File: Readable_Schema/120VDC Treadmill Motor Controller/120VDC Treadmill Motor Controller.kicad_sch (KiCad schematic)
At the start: 0 parts

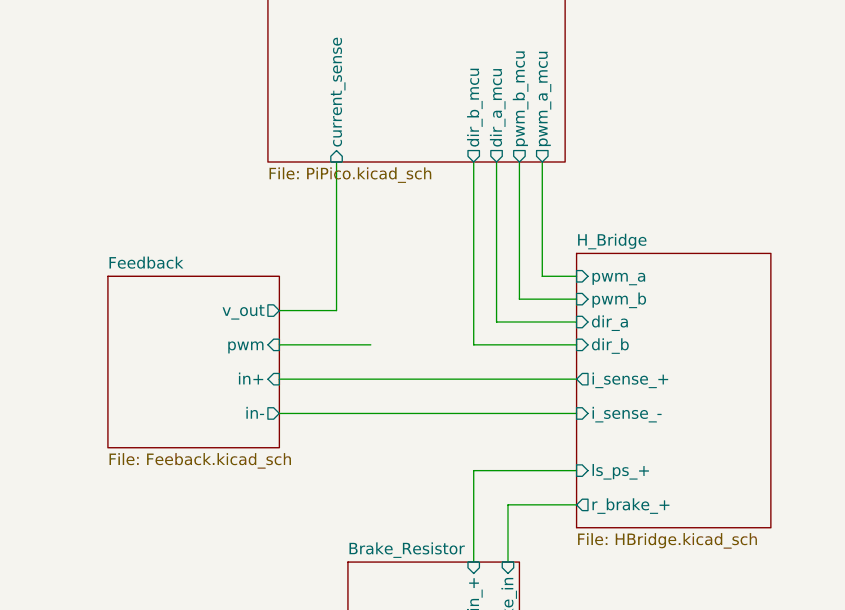
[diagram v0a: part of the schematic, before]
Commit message: -Tried to fix a decent portion of the feedback circuit. Basically the new gate drivers have a enable pin so it makes more sense to tie the OC pin directly to the function of EN. Also kept the SR latch as a method of delaying the restart and avoiding hysterysis -Still working through the brake resistor subcircuit, basically switching all comparator logic to HV and thinking of using optoisolation to feed comparator output to the gate driver to keep things isolated. Truthfully feels like I should just nuke that FOD3182 and use a bootstrap or something else since I could care less about isolation in that subcircuit since no communication with the microcontroller is needed.
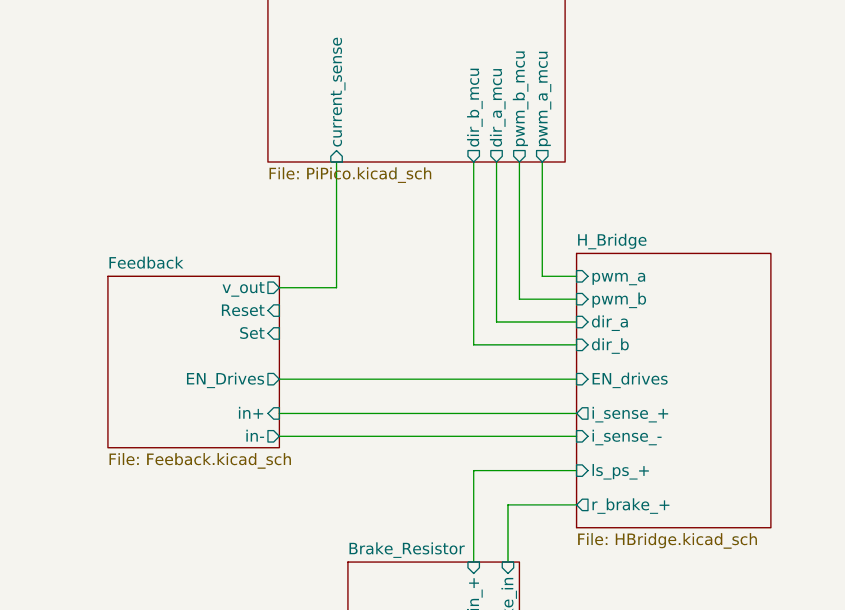
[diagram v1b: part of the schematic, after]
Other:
- sheet Feedback ports: added EN_Drives, Reset, Set; removed pwm
- sheet H_Bridge ports: added EN_drives; removed none
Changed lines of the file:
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@@
+	(wire
+		(pts
+			(xy 123.19 114.3) (xy 156.21 114.3)
+		)
+		(stroke
+			(width 0)
+			(type default)
+		)
+	)
+	(wire
+		(pts
+			(xy 123.19 97.79) (xy 129.54 97.79)
+		)
+		(stroke
+			(width 0)
+			(type default)
+		)
+	)
+	(wire
+		(pts
+			(xy 144.78 128.27) (xy 144.78 118.11)
+		)
+		(stroke
+			(width 0)
+			(type default)
+		)
+	)
+	(wire
+		(pts
+			(xy 144.78 104.14) (xy 156.21 104.14)
+		)
+		(stroke
+			(width 0)
+			(type default)
+		)
+	)
+	(wire
+		(pts
+			(xy 148.59 121.92) (xy 156.21 121.92)
+		)
+		(stroke
+			(width 0)
+			(type default)
+		)
+	)
+	(wire
+		(pts
+			(xy 152.4 83.82) (xy 152.4 96.52)
+		)
+		(stroke
+			(width 0)
+			(type default)
+		)
+	)
+	(wire
+		(pts
+			(xy 152.4 96.52) (xy 156.21 96.52)
+		)
+		(stroke
+			(width 0)
+			(type default)
+		)
+	)
+	(wire
+		(pts
+			(xy 147.32 101.6) (xy 156.21 101.6)
+		)
+		(stroke
+			(width 0)
+			(type default)
+		)
+	)
+	(wire
+		(pts
+			(xy 149.86 83.82) (xy 149.86 99.06)
+		)
+		(stroke
+			(width 0)
+			(type default)
+		)
+	)
+	(wire
+		(pts
+			(xy 144.78 83.82) (xy 144.78 104.14)
+		)
+		(stroke
+			(width 0)
+			(type default)
+		)
+	)
+	(wire
+		(pts
+			(xy 149.86 99.06) (xy 156.21 99.06)
+		)
+		(stroke
+			(width 0)
+			(type default)
+		)
+	)
+	(wire
+		(pts
+			(xy 147.32 83.82) (xy 147.32 101.6)
+		)
+		(stroke
+			(width 0)
+			(type default)
+		)
+	)
+	(wire
+		(pts
+			(xy 144.78 118.11) (xy 156.21 118.11)
+		)
+		(stroke
+			(width 0)
+			(type default)
+		)
+	)
+	(wire
+		(pts
+			(xy 129.54 83.82) (xy 129.54 97.79)
+		)
+		(stroke
+			(width 0)
+			(type default)
+		)
+	)
 	(wire
 		(pts
@@
 	(wire
 		(pts
-			(xy 123.19 100.33) (xy 129.54 100.33)
-		)
-		(stroke
-			(width 0)
-			(type default)
-		)
-	)
-	(wire
-		(pts
-			(xy 144.78 128.27) (xy 144.78 118.11)
-		)
-		(stroke
-			(width 0)
-			(type default)
-		)
-	)
-	(wire
-		(pts
-			(xy 144.78 104.14) (xy 156.21 104.14)
-		)
-		(stroke
-			(width 0)
-			(type default)
-		)
-	)
-	(wire
-		(pts
-			(xy 123.19 104.14) (xy 133.35 104.14)
-		)
-		(stroke
-			(width 0)
-			(type default)
-		)
-	)
-	(wire
-		(pts
-			(xy 148.59 121.92) (xy 156.21 121.92)
-		)
-		(stroke
-			(width 0)
-			(type default)
-		)
-	)
-	(wire
-		(pts
-			(xy 152.4 83.82) (xy 152.4 96.52)
-		)
-		(stroke
-			(width 0)
-			(type default)
-		)
-	)
-	(wire
-		(pts
-			(xy 152.4 96.52) (xy 156.21 96.52)
-		)
-		(stroke
-			(width 0)
-			(type default)
-		)
-	)
-	(wire
-		(pts
-			(xy 147.32 101.6) (xy 156.21 101.6)
-		)
-		(stroke
-			(width 0)
-			(type default)
-		)
-	)
-	(wire
-		(pts
-			(xy 149.86 83.82) (xy 149.86 99.06)
-		)
-		(stroke
-			(width 0)
-			(type default)
-		)
-	)
-	(wire
-		(pts
-			(xy 144.78 83.82) (xy 144.78 104.14)
-		)
-		(stroke
-			(width 0)
-			(type default)
-		)
-	)
-	(wire
-		(pts
-			(xy 149.86 99.06) (xy 156.21 99.06)
-		)
-		(stroke
-			(width 0)
-			(type default)
-		)
-	)
-	(wire
-		(pts
-			(xy 147.32 83.82) (xy 147.32 101.6)
+			(xy 148.59 128.27) (xy 148.59 121.92)
 		)
 		(stroke
@@
 		(pts
 			(xy 123.19 107.95) (xy 156.21 107.95)
-		)
-		(stroke
-			(width 0)
-			(type default)
-		)
-	)
-	(wire
-		(pts
-			(xy 144.78 118.11) (xy 156.21 118.11)
-		)
-		(stroke
-			(width 0)
-			(type default)
-		)
-	)
-	(wire
-		(pts
-			(xy 129.54 83.82) (xy 129.54 100.33)
-		)
-		(stroke
-			(width 0)
-			(type default)
-		)
-	)
-	(wire
-		(pts
-			(xy 148.59 128.27) (xy 148.59 121.92)
 		)
 		(stroke
@@
 		)
 		(pin "in+" input
+			(at 123.19 111.76 0)
+			(effects
+				(font
+					(size 1.27 1.27)
+				)
+				(justify right)
+			)
+		)
+		(pin "in-" output
+			(at 123.19 114.3 0)
+			(effects
+				(font
+					(size 1.27 1.27)
+				)
+				(justify right)
+			)
+		)
+		(pin "v_out" output
+			(at 123.19 97.79 0)
+			(effects
+				(font
+					(size 1.27 1.27)
+				)
+				(justify right)
+			)
+		)
+		(pin "EN_Drives" output
 			(at 123.19 107.95 0)
 			(effects
@@
 			)
 		)
-		(pin "in-" output
-			(at 123.19 111.76 0)
-			(effects
-				(font
-					(size 1.27 1.27)
-				)
-				(justify right)
-			)
-		)
-		(pin "pwm" input
-			(at 123.19 104.14 0)
-			(effects
-				(font
-					(size 1.27 1.27)
-				)
-				(justify right)
-			)
-		)
-		(pin "v_out" output
+		(pin "Reset" input
 			(at 123.19 100.33 0)
+			(effects
+				(font
+					(size 1.27 1.27)
+				)
+				(justify right)
+			)
+		)
+		(pin "Set" input
+			(at 123.19 102.87 0)
 			(effects
 				(font
@@
 		)
 		(pin "i_sense_+" output
-			(at 156.21 107.95 180)
+			(at 156.21 111.76 180)
 			(effects
 				(font
@@
 		)
 		(pin "i_sense_-" input
-			(at 156.21 111.76 180)
+			(at 156.21 114.3 180)
 			(effects
 				(font
@@
 			(effects
 				(font
+					(size 1.27 1.27)
+				)
+				(justify left)
+			)
+		)
+		(pin "EN_drives" input
+			(at 156.21 107.95 180)
+			(effects
+				(font

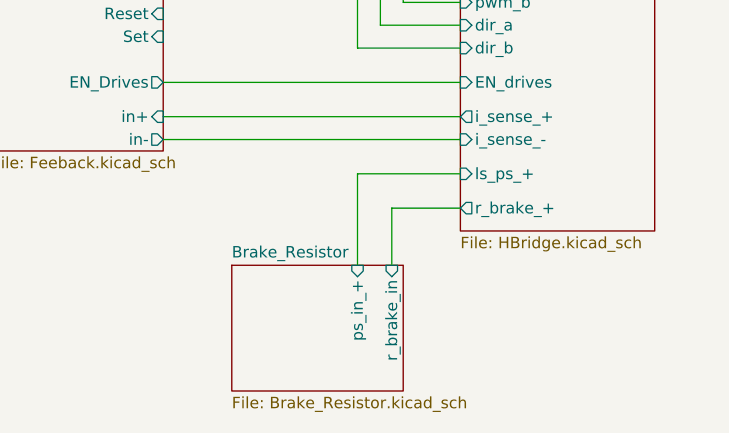
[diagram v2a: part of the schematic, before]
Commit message: -Removed brake resistor subcircuit -Worked up bus cap to 4x 820uF 400V caps -changed the fets to 600V 49A 60mOhm RdsON --------------------------------------------- -need different isolated power supplies --May want to consider a bootstrap circuit since we wont be needing 100% duty cycle -need to resize gate resistors -Need to change out bridge rectifier to be vertical for ease of mounting heatsink
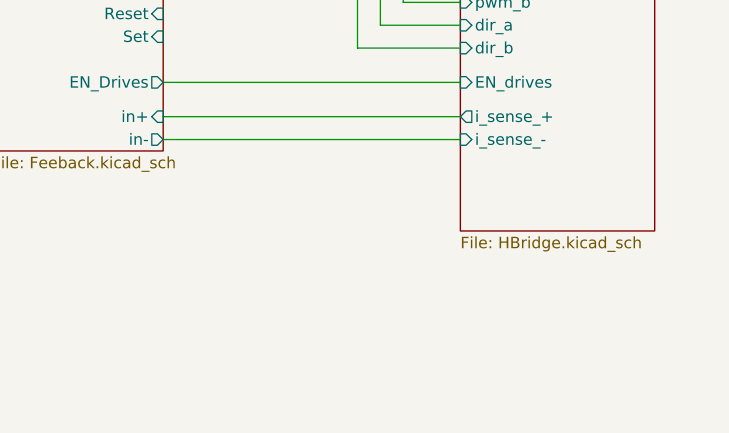
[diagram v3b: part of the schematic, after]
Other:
- removed sheet Brake_Resistor
- sheet H_Bridge ports: added none; removed ls_ps_+, r_brake_+
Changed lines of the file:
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@@
-	(wire
-		(pts
-			(xy 144.78 128.27) (xy 144.78 118.11)
-		)
-		(stroke
-			(width 0)
-			(type default)
-		)
-	)
 	(wire
 		(pts
@@
 	(wire
 		(pts
-			(xy 148.59 121.92) (xy 156.21 121.92)
-		)
-		(stroke
-			(width 0)
-			(type default)
-		)
-	)
-	(wire
-		(pts
 			(xy 152.4 83.82) (xy 152.4 96.52)
 		)
@@
 	(wire
 		(pts
-			(xy 144.78 118.11) (xy 156.21 118.11)
-		)
-		(stroke
-			(width 0)
-			(type default)
-		)
-	)
-	(wire
-		(pts
 			(xy 129.54 83.82) (xy 129.54 97.79)
 		)
@@
 		(pts
 			(xy 123.19 111.76) (xy 156.21 111.76)
-		)
-		(stroke
-			(width 0)
-			(type default)
-		)
-	)
-	(wire
-		(pts
-			(xy 148.59 128.27) (xy 148.59 121.92)
 		)
 		(stroke
@@
 			)
 		)
-		(pin "r_brake_+" output
-			(at 156.21 121.92 180)
-			(effects
-				(font
-					(size 1.27 1.27)
-				)
-				(justify left)
-			)
-		)
 		(pin "dir_a" input
 			(at 156.21 101.6 180)
@@
 		(pin "dir_b" input
 			(at 156.21 104.14 180)
-			(effects
-				(font
-					(size 1.27 1.27)
-				)
-				(justify left)
-			)
-		)
-		(pin "ls_ps_+" input
-			(at 156.21 118.11 180)
 			(effects
 				(font
@@
 				)
 			)
-		)
-	)
-	(sheet
-		(at 130.81 128.27)
-		(size 19.05 13.97)
-		(exclude_from_sim no)
-		(in_bom yes)
-		(on_board yes)
-		(dnp no)
-		(fields_autoplaced yes)
-		(stroke
-			(width 0.1524)
-			(type solid)
-		)
-		(fill
-			(color 0 0 0 0.0000)
-		)
-		(property "Sheetname" "Brake_Resistor"
-			(at 130.81 127.5584 0)
-			(effects
-				(font
-					(size 1.27 1.27)
-				)
-				(justify left bottom)
-			)
-		)
-		(property "Sheetfile" "Brake_Resistor.kicad_sch"
-			(at 130.81 142.8246 0)
-			(effects
-				(font
-					(size 1.27 1.27)
-				)
-				(justify left top)
-			)
-		)
-		(pin "r_brake_in" input
-			(at 148.59 128.27 90)
-			(effects
-				(font
-					(size 1.27 1.27)
-				)
-				(justify right)
-			)
-		)
-		(pin "ps_in_+" input
-			(at 144.78 128.27 90)
-			(effects
-				(font
-					(size 1.27 1.27)
-				)
-				(justify right)
-			)
-		)
-		(instances
-			(project "120VDC Treadmill Motor Controller"
-				(path "/319bc5c0-2dd5-4df3-a34b-9170833ebccd"
-					(page "10")
-				)
-			)

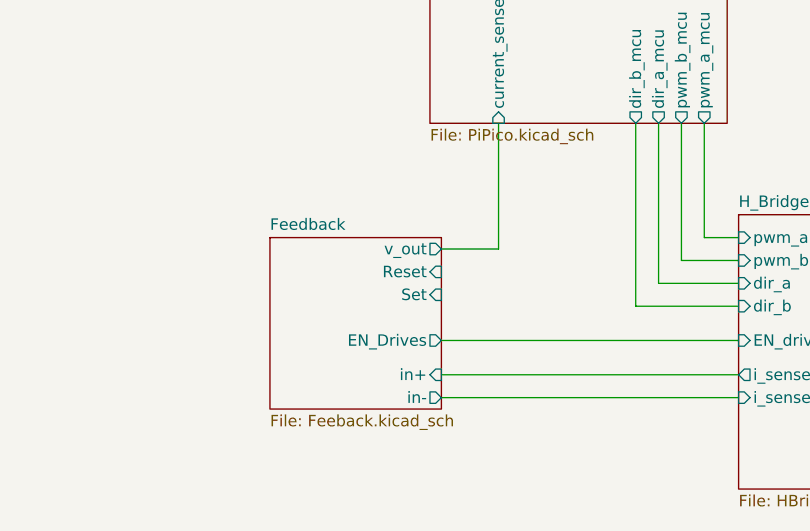
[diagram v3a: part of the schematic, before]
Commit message: -changed the feedback loop to use a and gate rather than a SR latch, were also back to not needing any input from the mcu for the whole OC protection --missing a footprint for the and gate chip -Still missing a full precharge circuit on the caps. debating internally whether to use fets with a gate driver or something of that nature vs a relay to do this. Trying to minimize board space for this given the current size of everything
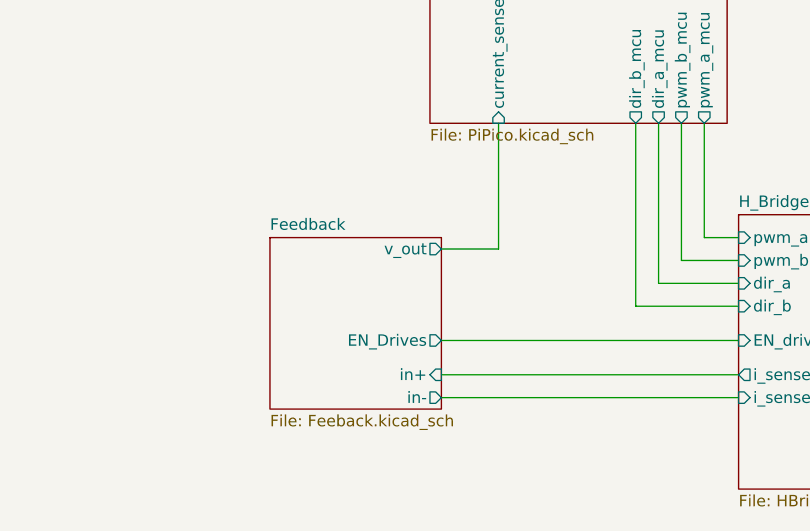
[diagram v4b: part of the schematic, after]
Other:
- sheet Feedback ports: added none; removed Reset, Set
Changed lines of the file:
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@@
-			)
-		)
-		(pin "Reset" input
-			(at 123.19 100.33 0)
-			(effects
-				(font
-					(size 1.27 1.27)
-				)
-				(justify right)
-			)
-		)
-		(pin "Set" input
-			(at 123.19 102.87 0)
-			(effects
-				(font
-					(size 1.27 1.27)
-				)
-				(justify right)
 			)
 		)

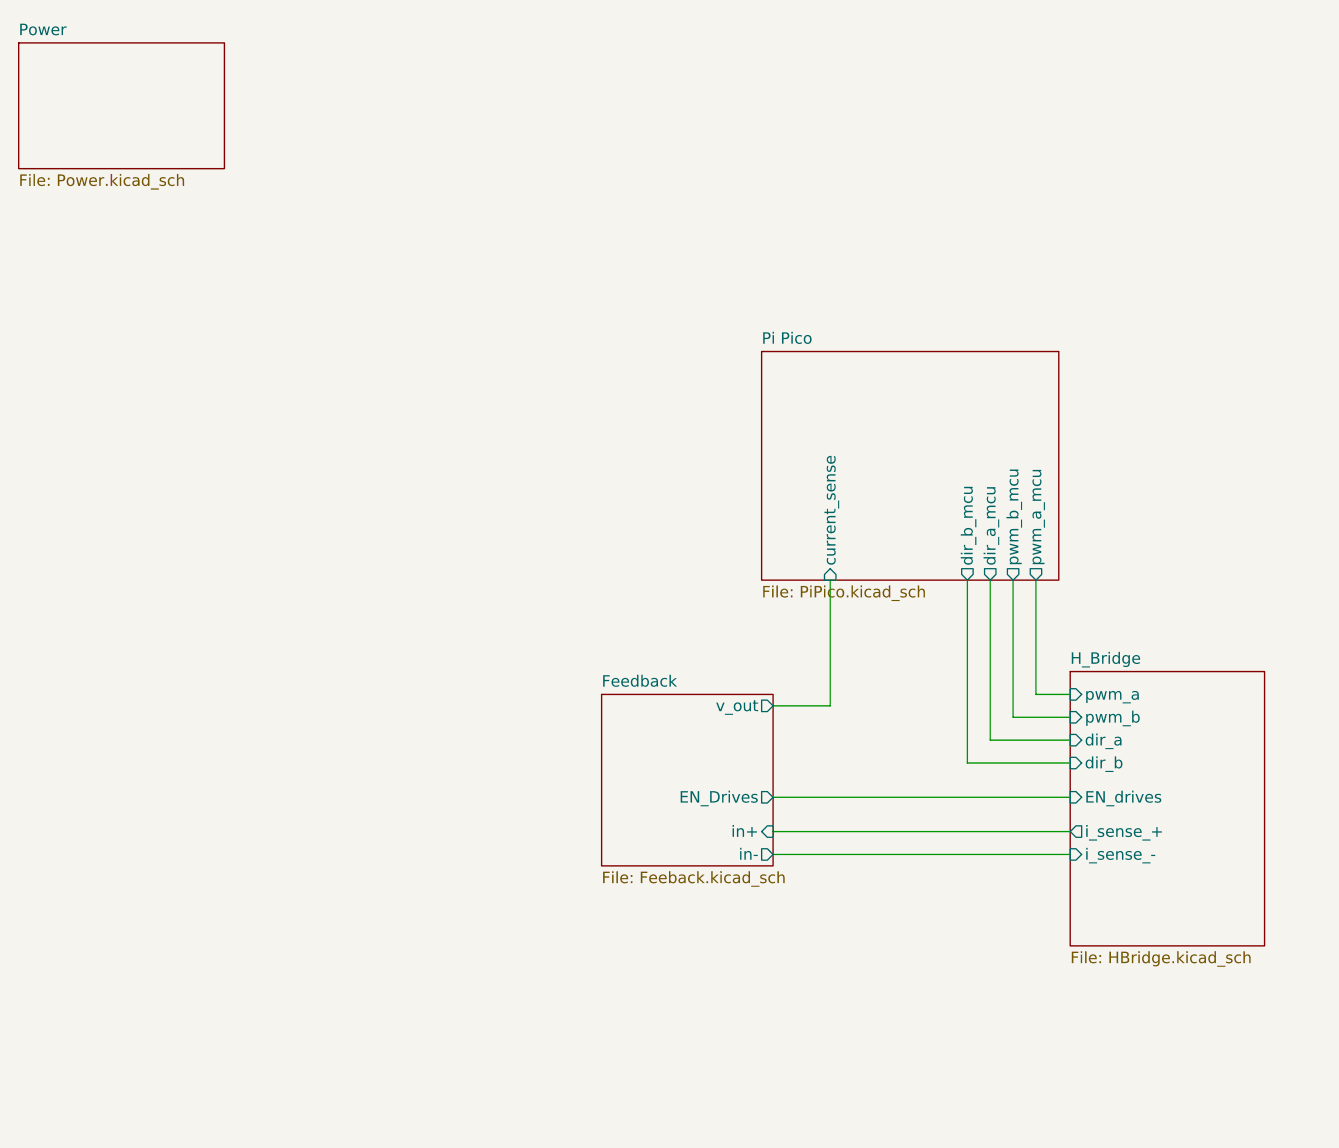
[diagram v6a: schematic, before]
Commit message: -Changed the precharge circuit gate driver to the TP5I3 --This gate driver provides its own 10v isolated PS, which saves a lot of room
-changed the schottky for the pi pico to a smd equivalent.
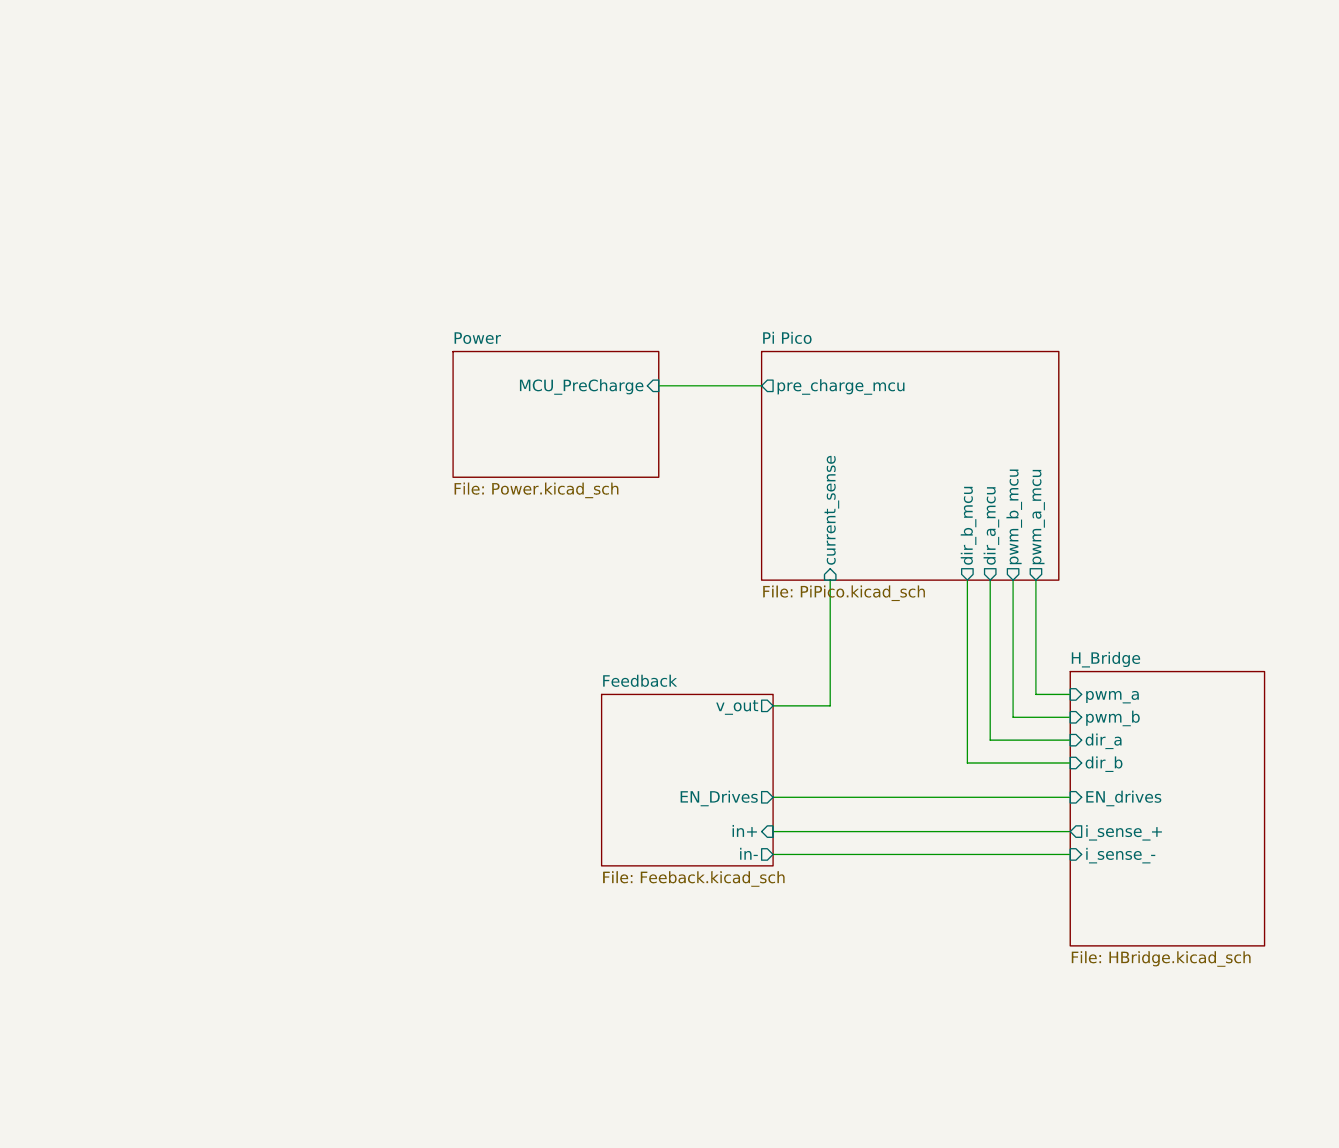
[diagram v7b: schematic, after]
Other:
- sheet Pi Pico ports: added pre_charge_mcu; removed none
- sheet Power ports: added MCU_PreCharge; removed none
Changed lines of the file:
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@@
+	(wire
+		(pts
+			(xy 110.49 62.23) (xy 121.92 62.23)
+		)
+		(stroke
+			(width 0)
+			(type default)
+		)
+	)
 	(wire
 		(pts
@@
 	)
 	(sheet
-		(at 39.37 24.13)
+		(at 87.63 58.42)
 		(size 22.86 13.97)
 		(exclude_from_sim no)
@@
 		)
 		(property "Sheetname" "Power"
-			(at 39.37 23.4184 0)
+			(at 87.63 57.7084 0)
 			(effects
 				(font
@@
 		)
 		(property "Sheetfile" "Power.kicad_sch"
-			(at 39.37 38.6846 0)
+			(at 87.63 72.9746 0)
 			(effects
 				(font
@@
 				)
 				(justify left top)
+			)
+		)
+		(pin "MCU_PreCharge" input
+			(at 110.49 62.23 0)
+			(effects
+				(font
+					(size 1.27 1.27)
+				)
+				(justify right)
 			)
 		)
@@
 			(effects
 				(font
+					(size 1.27 1.27)
+				)
+				(justify left)
+			)
+		)
+		(pin "pre_charge_mcu" output
+			(at 121.92 62.23 180)
+			(effects
+				(font
